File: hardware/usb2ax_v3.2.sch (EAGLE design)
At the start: 28 parts, among them Q1 CRYSTAL-0500290P1, U1 ATmega32u2, U2 IPC4282CZ6

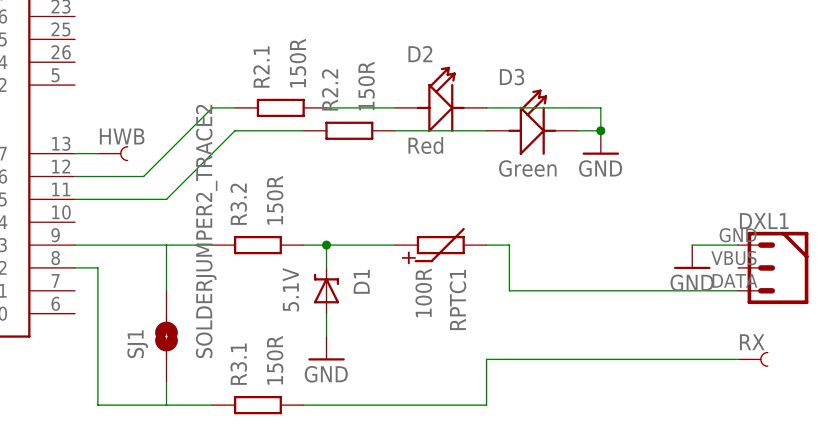
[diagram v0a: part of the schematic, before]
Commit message: Upgraded to v3.2b : changed R3 from 150 to 47ohms for stronger line drive
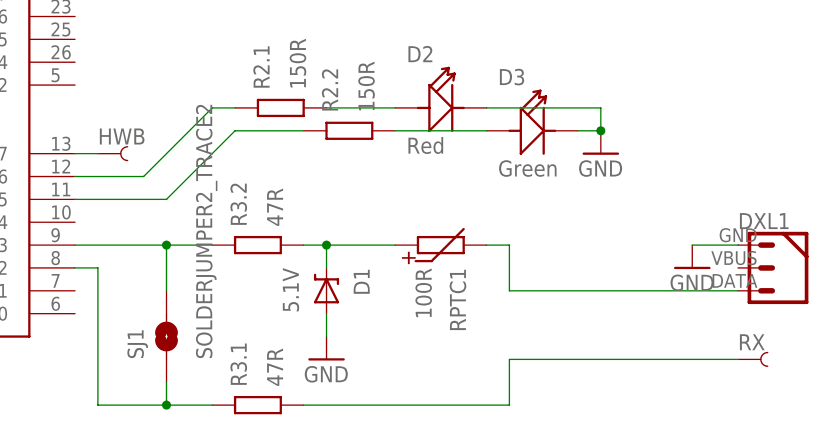
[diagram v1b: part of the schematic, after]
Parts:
- R3: value 150R -> 47R
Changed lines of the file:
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@@
 <?xml version="1.0" encoding="utf-8"?>
 <!DOCTYPE eagle SYSTEM "eagle.dtd">
-<eagle version="6.5.0">
+<eagle version="7.5.0">
 <drawing>
 <settings>
@@
 <part name="R1" library="Xevelabs" deviceset="R_2" device="-0402" value="22R"/>
 <part name="R2" library="Xevelabs" deviceset="R_2" device="-0402" value="150R"/>
-<part name="R3" library="Xevelabs" deviceset="R_2" device="-0402" value="150R"/>
+<part name="R3" library="Xevelabs" deviceset="R_2" device="-0402" value="47R"/>
 <part name="U2" library="Xevelabs" deviceset="IPC4282CZ6" device=""/>
 <part name="GND6" library="supply1" deviceset="GND" device=""/>
@@
 <wire x1="139.7" y1="60.96" x2="139.7" y2="55.88" width="0.1524" layer="91"/>
 <pinref part="SJ1" gate="1" pin="2"/>
+<junction x="139.7" y="60.96"/>
 </segment>
 </net>
@@
 <wire x1="139.7" y1="43.18" x2="139.7" y2="45.72" width="0.1524" layer="91"/>
 <pinref part="SJ1" gate="1" pin="1"/>
+<junction x="139.7" y="43.18"/>
 </segment>
 </net>
@@
 <segment>
 <pinref part="R3" gate=".1" pin="1"/>
-<wire x1="154.94" y1="43.18" x2="175.26" y2="43.18" width="0.1524" layer="91"/>
-<wire x1="175.26" y1="43.18" x2="175.26" y2="48.26" width="0.1524" layer="91"/>
-<wire x1="175.26" y1="48.26" x2="203.2" y2="48.26" width="0.1524" layer="91"/>
+<wire x1="154.94" y1="43.18" x2="177.8" y2="43.18" width="0.1524" layer="91"/>
+<wire x1="177.8" y1="43.18" x2="177.8" y2="48.26" width="0.1524" layer="91"/>
+<wire x1="177.8" y1="48.26" x2="203.2" y2="48.26" width="0.1524" layer="91"/>
 <pinref part="RX" gate="G$1" pin="1"/>
 </segment>
